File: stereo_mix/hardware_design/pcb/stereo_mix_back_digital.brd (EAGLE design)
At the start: 70 x 100 mm, 220 parts, among them IC1 4051CD4051, IC2 AMS1117-3.3, J1 WQP-PJ301M-12_JACK, J10 WQP-PJ301M-12_JACK, J11 WQP-PJ301M-12_JACK, J12 WQP-PJ301M-12_JACK, J13 WQP-PJ301M-12_JACK, J14 WQP-PJ301M-12_JACK, J15 WQP-PJ301M-12_JACK, J16 WQP-PJ301M-12_JACK, J17 CORTEX_DEBUG_PTH, J18 WQP-PJ301M-12_JACK, J19 WQP-PJ301M-12_JACK, J2 WQP-PJ301M-12_JACK, J3 WQP-PJ301M-12_JACK, J4 WQP-PJ301M-12_JACK, J5 WQP-PJ301M-12_JACK, J6 WQP-PJ301M-12_JACK, J7 WQP-PJ301M-12_JACK, J8 WQP-PJ301M-12_JACK, J9 WQP-PJ301M-12_JACK, U1 MCP4822E-SN, U10 MCP4822E-SN, U11 MCP6002T-I/SN, U12 MCP6002T-I/SN, U13 MCP4922E/SL, U14 MCP4922E/SL, U15 TL072CD, U16 TL072CD, U17 MCP6002T-I/SN, U18 MCP6002T-I/SN, U19 MCP6002T-I/SN, U2 MCP4822E-SN, U20 MCP6002T-I/SN, U21 STM32F030C8T6, U22 TL072CD, U3 MCP6002T-I/SN, U4 MCP6002T-I/SN, U5 MCP4922E/SL, U6 MCP4922E/SL, U7 TL072CD, U8 TL072CD, U9 MCP4822E-SN, X1 8MHz

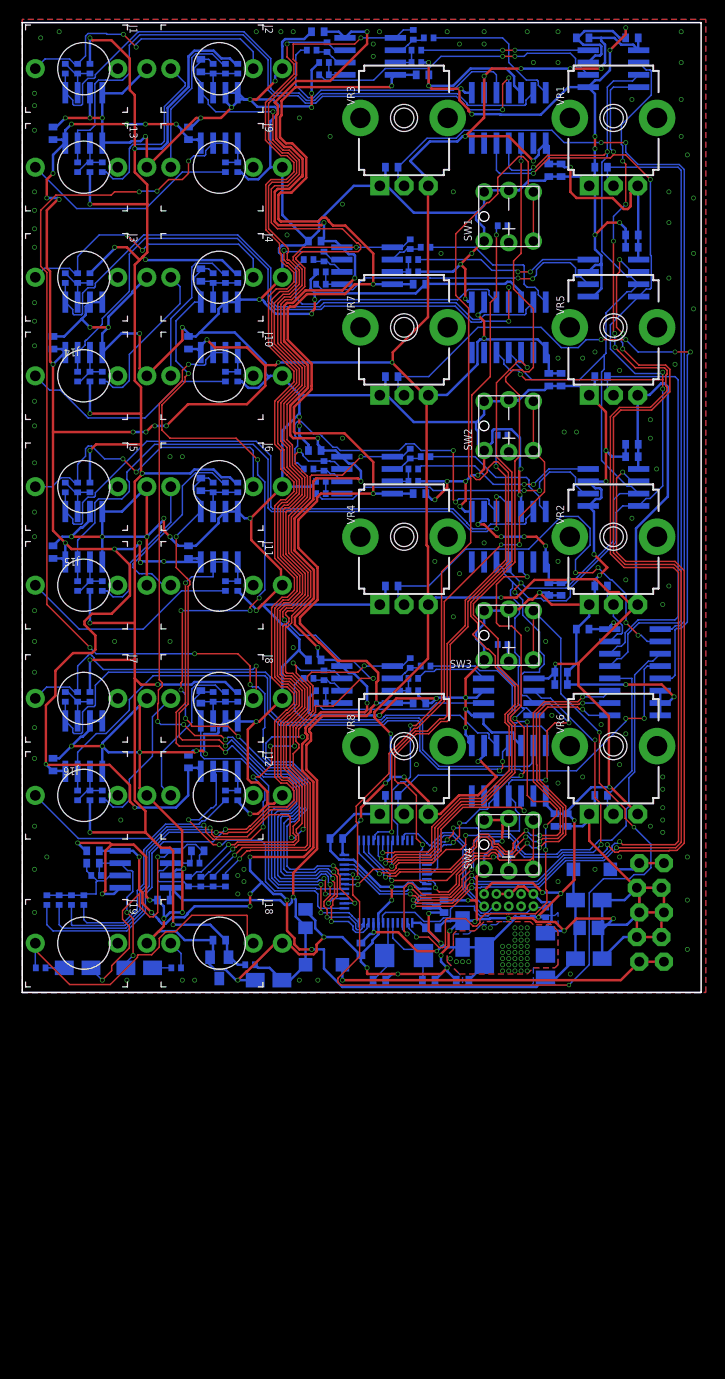
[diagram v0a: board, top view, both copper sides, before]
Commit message: Fix problem in stereo_mix dac
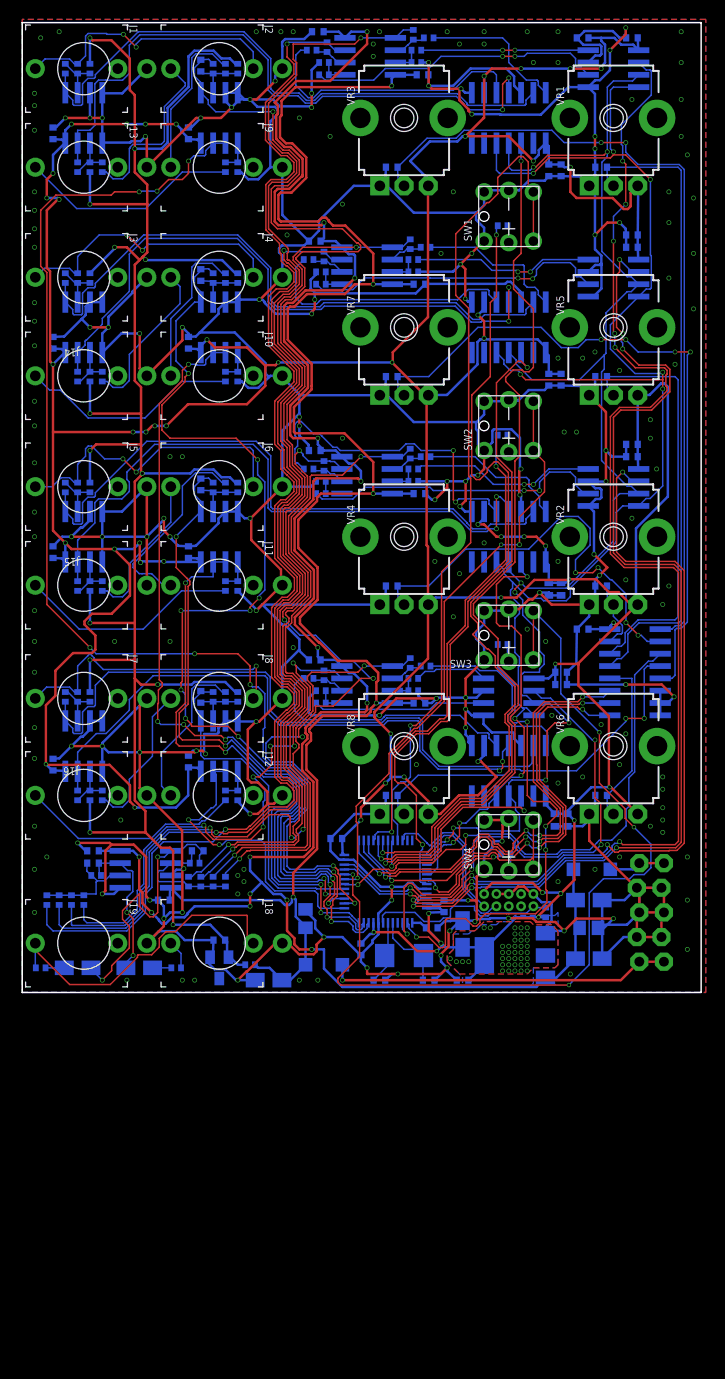
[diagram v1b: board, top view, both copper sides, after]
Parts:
- C1, C10, C11, C12, C13, C14, C15, C16, C17, C18, C19, C2, C20, C21, C22, C23, C24, C25, C26, C27, C28, C29, C3, C30, C31, C32, C33, C34, C35, C4, C40, C42, C43, C44, C49, C5, C50, C53, C54, C55, C56, C57, C58, C59, C6, C60, C61, C62, C63, C64, C7, C8, C9: device jhbruhn-cr:C0402 -> jhbruhn-cdr:C0402
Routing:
- net GND: track 968.1 -> 968.7 mm

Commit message: Hardware filtering improvements
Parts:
- added C67, C68, C69, C70, C71, C72, C73, C74: 1uF, jhbruhn-cdr:C0402
- added R86, R87: 47k, jhbruhn-cdr:R0402
- C49, C50, C53, C54, C55, C56: device jhbruhn-cdr:C0402 -> jhbruhn-cdr:C0805
- C51, C52: device jhbruhn-cr:C0402 -> jhbruhn-cdr:C0805
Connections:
- net BIAS_DAC1_L: now also C69.1
- net BIAS_DAC1_R: now also C70.1
- net BIAS_DAC2_L: now also C67.1
- net BIAS_DAC2_R: now also C68.1
- net BIAS_DAC3_L: now also C71.1
- net BIAS_DAC3_R: now also C72.1
- net BIAS_DAC4_L: now also C73.1
- net BIAS_DAC4_R: now also C74.1
- net GND: now also C67.2, C68.2, C69.2, C70.2, C71.2, C72.2, C73.2, C74.2, R86.1, R87.1
- net N$45: now also R86.2
- net N$57: now also R87.2
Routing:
- net GND: track 968.7 -> 0.00 mm, vias 202 -> 0
- net +3V3: track 570.2 -> 569.3 mm

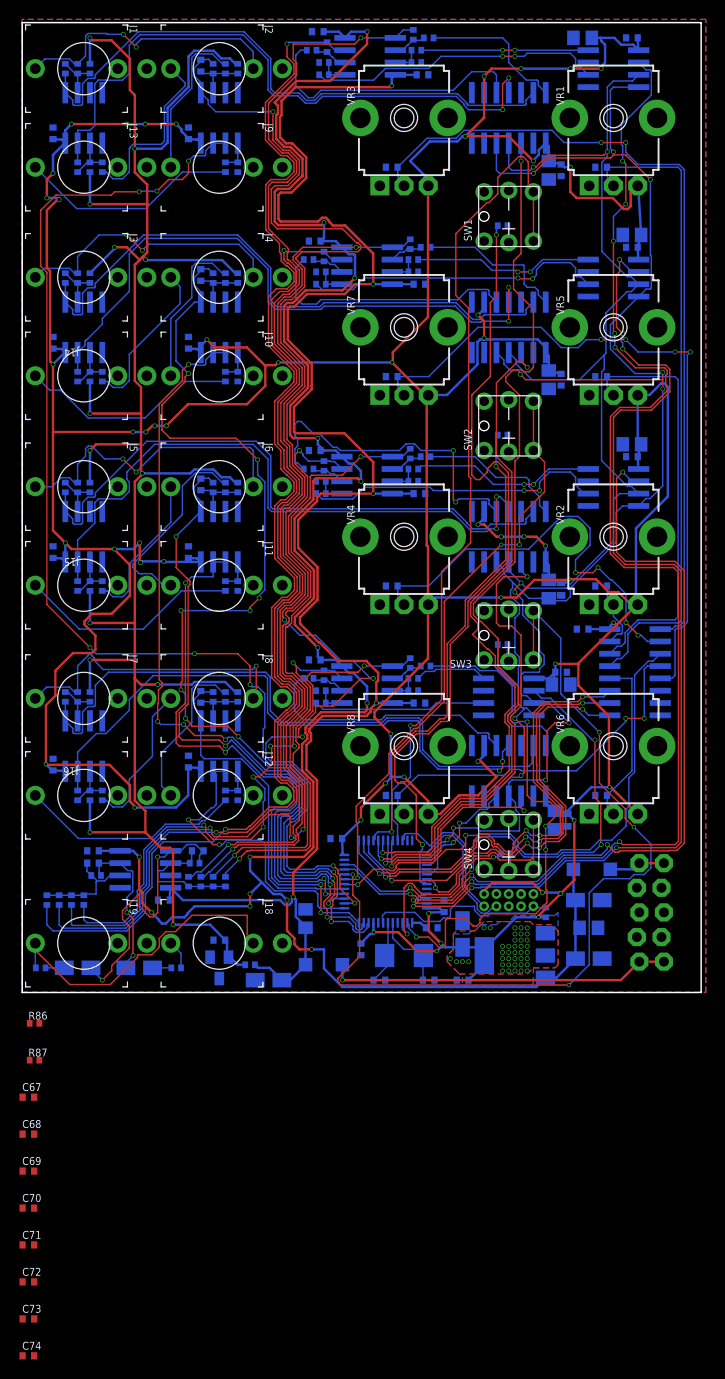
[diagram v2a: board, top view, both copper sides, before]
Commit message: Update stereo_mix to new hardware revision
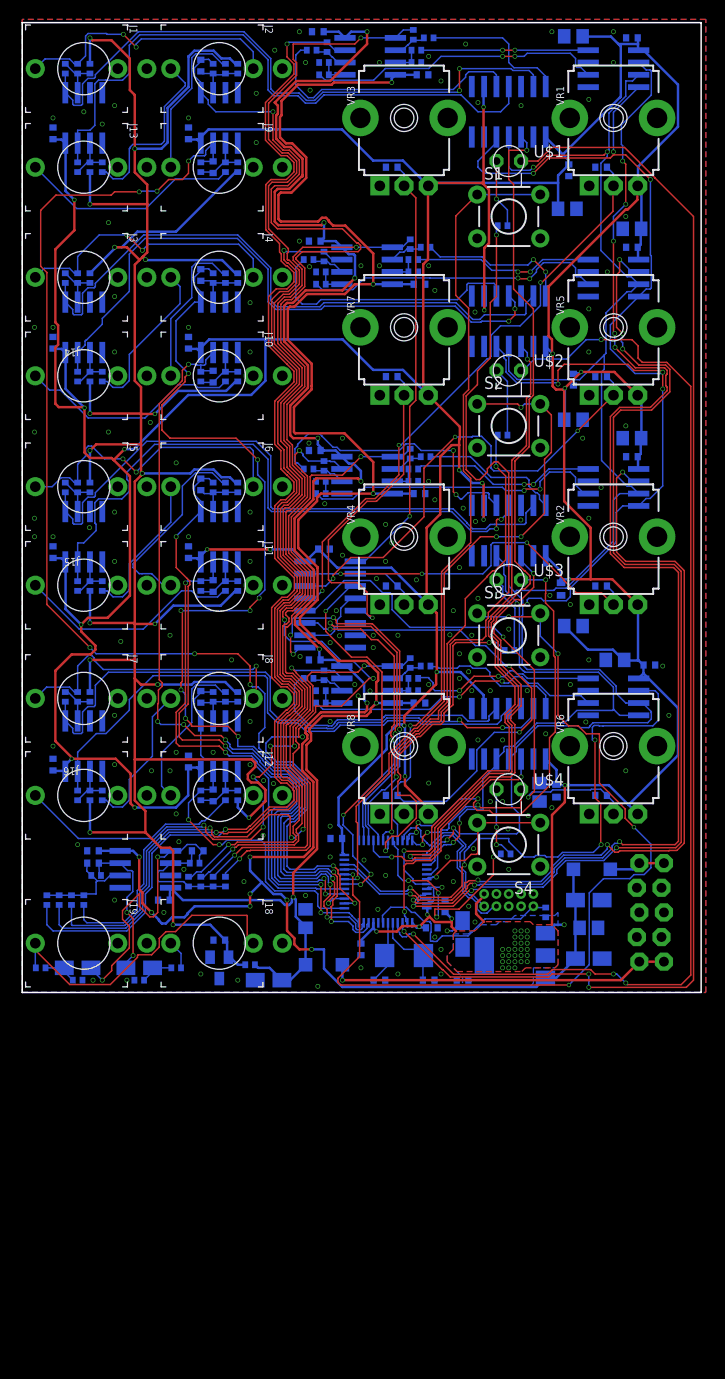
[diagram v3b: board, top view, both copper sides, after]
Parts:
- removed C71, C72, C73, C74: 1uF, jhbruhn-cdr:C0402
- removed SW1, SW2, SW3, SW4: (no value), jhbruhn-physical:PB6149L
- added R100, R97, R98, R99: 20k, jhbruhn-cr:R0402
- added S1, S2, S3, S4: (no value), jhbruhn-physical:TACTILE-PTH
- added U$1, U$2, U$3, U$4: LED-BICOLOR-SHARED-THROUGHHOLE, jhbruhn-physical:LED3MM
- C19, C20, C21, C22: value 4.7nF -> 1.0nF
- C67, C68, C69, C70: value 1uF -> 1.0nF
- R101, R81, R82, R83: value 100k -> 120k
- R65, R67, R69, R71: value 200k -> 120k
- R73, R74, R75, R76: value 33k -> 20k
- VR1, VR2, VR3, VR4, VR5, VR6, VR7, VR8: value (none) -> 10k
- moved C67 97.8 mm to (19.7, 85.1), flipped to the bottom, turned to 90 degrees
- moved C68 80.4 mm to (19.7, 63.5), flipped to the bottom, turned to 90 degrees
- moved C69 63.3 mm to (19.7, 41.9), flipped to the bottom, turned to 90 degrees
- moved C70 46.6 mm to (19.7, 20.3), flipped to the bottom, turned to 90 degrees
- moved IC1 32.2 mm to (31.8, 40.0)
- moved C31 27.9 mm to (31.1, 45.7), turned to 180 degrees
- moved LOGO1 19.0 mm to (49.9, 32.9)
- moved R87 13.6 mm to (12.1, 1.27), flipped to the bottom, turned to 180 degrees
- moved U10 10.8 mm to (61.0, 30.5)
- moved C13 9.13 mm to (64.7, 33.8)
- moved R86 6.29 mm to (5.71, 1.27), flipped to the bottom
- moved C56 6.11 mm to (61.1, 34.3), turned to 0 degrees
- moved C50 4.85 mm to (56.8, 59.1), turned to 180 degrees
- moved C51 4.58 mm to (56.8, 37.8), turned to 180 degrees
- moved C49 4.40 mm to (56.2, 80.8), turned to 180 degrees
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- renumbered R84 to R101
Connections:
- removed net N$66: R79.1, R83.2, U19.5
- removed net N$69: R101.2, R80.1, U20.5
- new net LED_1_N: U$1.2, U21.3
- new net LED_2_N: U$2.2, U21.4
- new net LED_3_N: U$3.2, U21.35
- new net LED_4_N: U$4.2, U21.36
- new net N$65: C67.1, R77.1, R81.2, R97.1, U17.6
- new net N$74: C68.1, R78.1, R82.2, R98.1, U18.6
- net AREF_-10: now also R101.1, R81.1, R82.1, R83.1
- net BIAS_DAC1_L: no longer C69.1
- net BIAS_DAC1_R: no longer C70.1
- net BIAS_DAC2_L: no longer C67.1
- net BIAS_DAC2_R: no longer C68.1
- net BIAS_DAC3_L: no longer C71.1
- net BIAS_DAC3_R: no longer C72.1
- net BIAS_DAC4_L: no longer C73.1
- net BIAS_DAC4_R: no longer C74.1
- net CS_DAC_1: now also U21.38; no longer U21.29
- net CS_DAC_2: now also U21.43; no longer U21.30
- net CS_DAC_3: now also U21.28; no longer U21.31
- net CS_DAC_4: now also U21.2; no longer U21.32
- net GND: now also S1.3, S1.4, S2.3, S2.4, S3.3, S3.4, S4.1, S4.2, U17.5, U18.5, U19.5, U20.5; no longer C67.2, C68.2, C69.2, C70.2, C71.2, C72.2, C73.2, C74.2, R101.1, R81.1, R82.1, R83.1, SW1.3, SW1.4, SW1.K, SW2.3, SW2.4, SW2.K, SW3.3, SW3.4, SW3.K, SW4.3, SW4.4, SW4.K
- net LED_1: now also U21.29; no longer U21.43
- net LED_2: now also U21.30; no longer U21.28
- net LED_3: now also U21.31; no longer U21.2
- net LED_4: now also U21.32; no longer U21.3
- net N$12: now also U$1.1; no longer SW1.A
- net N$13: now also U$2.1; no longer SW2.A
- net N$15: now also C69.1, R79.1, R83.2, R99.1, U19.6; no longer R77.1, R81.2, U17.5
- net N$17: now also C70.1, R100.1, R101.2, R80.1, U20.6; no longer R78.1, R82.2, U18.5
- net N$18: now also U$3.1; no longer SW3.A
- net N$42: now also U$4.1; no longer SW4.A
- net SWITCH_1: now also S1.1, S1.2; no longer SW1.1, SW1.2
- net SWITCH_2: now also S2.1, S2.2; no longer SW2.1, SW2.2
- net SWITCH_3: now also S3.1, S3.2; no longer SW3.1, SW3.2
- net SWITCH_4: now also S4.3, S4.4; no longer SW4.1, SW4.2
- net VOL_CV_1: now also C67.2, R97.2; no longer U17.6
- net VOL_CV_2: now also C68.2, R98.2; no longer U18.6
- net VOL_CV_3: now also C69.2, R99.2; no longer U19.6
- net VOL_CV_4: now also C70.2, R100.2; no longer U20.6
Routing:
- net LED_1_N: track 0.00 -> 134.6 mm, vias 0 -> 3
- net LED_2_N: track 0.00 -> 116.7 mm, vias 0 -> 4
- net AREF_-10: track 221.7 -> 283.7 mm, vias 13 -> 16
- net LED_3_N: track 0.00 -> 44.8 mm, vias 0 -> 4
- net PAN_1_POT: track 85.0 -> 44.6 mm, vias 2 -> 1
- net PAN_2_POT: track 72.1 -> 34.6 mm, vias 4 -> 1
- net PAN_3_POT: track 44.6 -> 7.07 mm, vias 4 -> 0
- net VOL_4_POT: track 17.6 -> 54.2 mm, vias 0 -> 2
- net +3V3: track 569.3 -> 602.2 mm, vias 93 -> 52
- net VOL_3_POT: track 7.15 -> 39.3 mm, vias 0 -> 3
- net MOSI: track 152.9 -> 173.5 mm
- net MUX_ADDR_0: track 49.8 -> 31.4 mm, vias 4 -> 2
- net LED_3: track 52.1 -> 34.7 mm, vias 4 -> 2
- net LED_4_N: track 0.00 -> 15.8 mm, vias 0 -> 3
- net MUX_ADDR_1: track 49.1 -> 33.4 mm, vias 4 -> 2
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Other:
- board text added: "/home/jhbruhn/Downloads/260322bfe49b091852bc7901a328687b.bmp"
- board text added: "stereo_mix v5"
- board text removed: "stereo_mix v4"
